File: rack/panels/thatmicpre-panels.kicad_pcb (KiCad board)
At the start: 2 copper layers, 87.9 x 78 mm, 2 parts

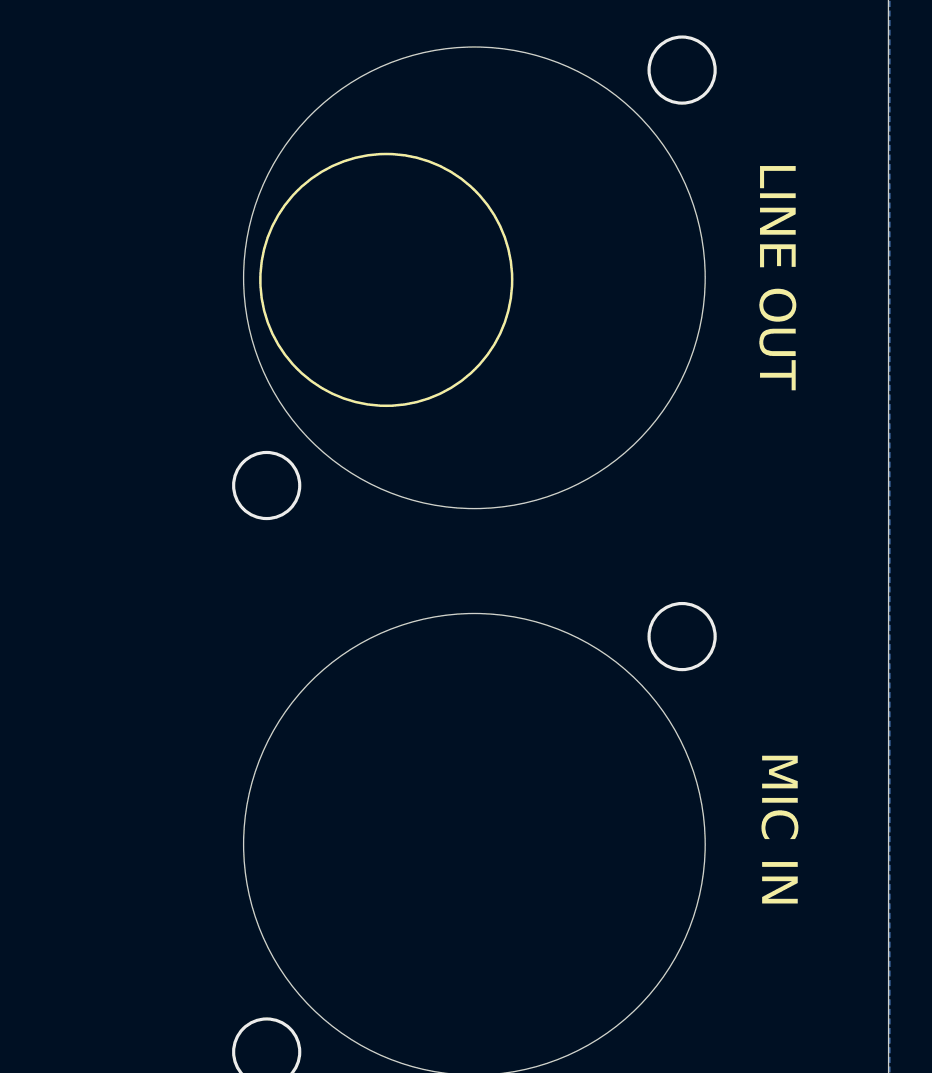
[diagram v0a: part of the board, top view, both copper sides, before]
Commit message: Modified rack version BOM to match assembled prototype
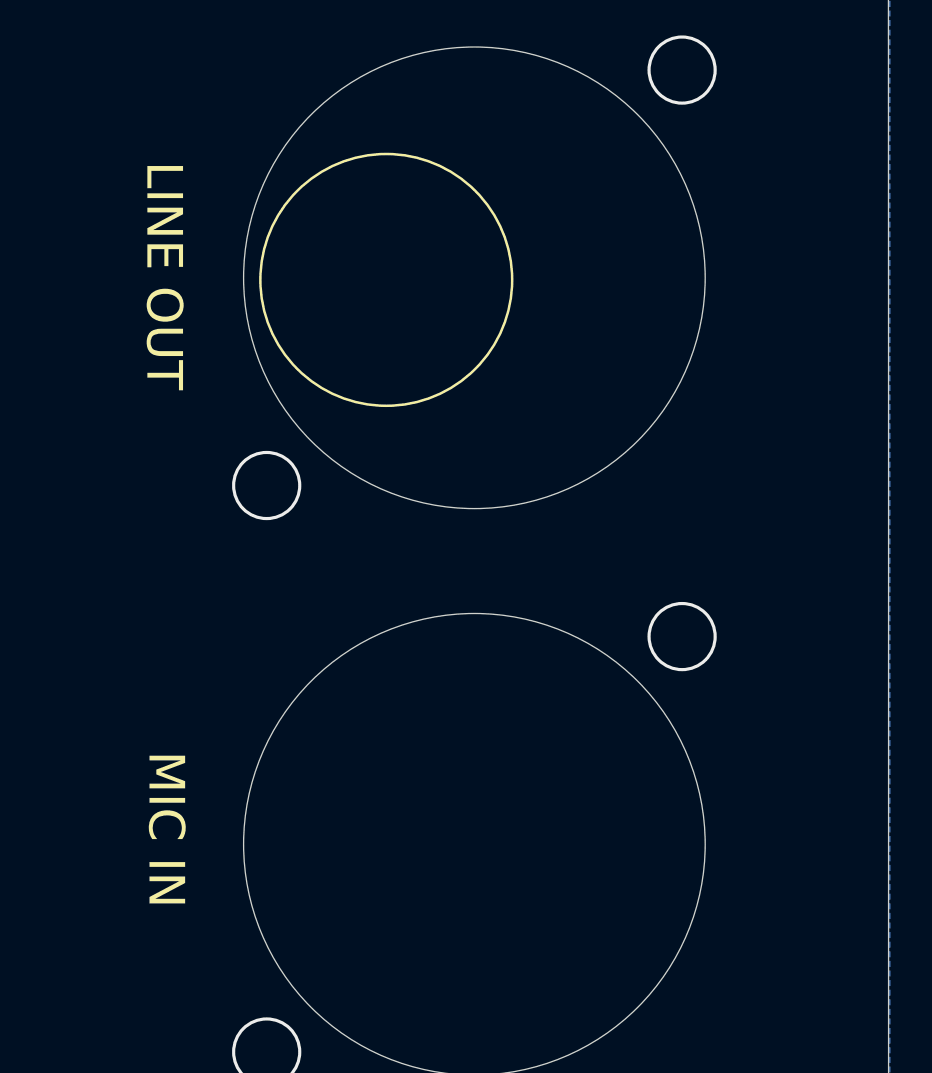
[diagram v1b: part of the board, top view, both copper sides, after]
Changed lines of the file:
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@@
     (effects (font (size 2.5 2.5) (thickness 0.4)) (justify left))
   )
-  (gr_text "MIC IN" (at 185.387984 112.295736 270) (layer "F.SilkS")
+  (gr_text "MIC IN" (at 156.187984 112.295736 270) (layer "F.SilkS")
     (effects (font (size 1.7 1.7) (thickness 0.27)))
   )
@@
     (effects (font (size 1.7 1.7) (thickness 0.27)))
   )
-  (gr_text "LINE OUT" (at 185.287984 85.895736 270) (layer "F.SilkS")
+  (gr_text "LINE OUT" (at 156.087984 85.895736 270) (layer "F.SilkS")
     (effects (font (size 1.7 1.7) (thickness 0.27)))
   )
